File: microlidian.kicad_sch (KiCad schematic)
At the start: 31 parts, among them J1 Conn_02x05_Odd_Even, J11 Backboard Conn 1, J12 Frontboard Conn 1, J13 Backboard Conn 2, J14 Frontboard Conn 2, J2 ST7789 TFT socket, J3 Expansion header, J4 ADS1015 digital side, J5 ADS1015 analog side, J7 TRS MIDI Out, SW1 RotaryEncoder_Switch, SW2 Back button, U1 SeeeduinoXIAO, U2 L78L05_TO92

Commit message: some minor updates
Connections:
- net GND: no longer J5.5 (Pin_5)
- new net CV GND: J5.5 (Pin_5)
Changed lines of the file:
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@@
     )
   )
-  (global_label "CV GND" (shape input) (at 180.848 20.32 0) (fields_autoplaced)
+  (global_label "CV GND" (shape input) (at 200.406 20.32 0) (fields_autoplaced)
     (effects (font (size 1.27 1.27)) (justify left))
-    (property "Intersheetrefs" "${INTERSHEET_REFS}" (at 190.0907 20.32 0)
+    (property "Intersheetrefs" "${INTERSHEET_REFS}" (at 209.6487 20.32 0)
       (effects (font (size 1.27 1.27)) (justify left) hide)
     )

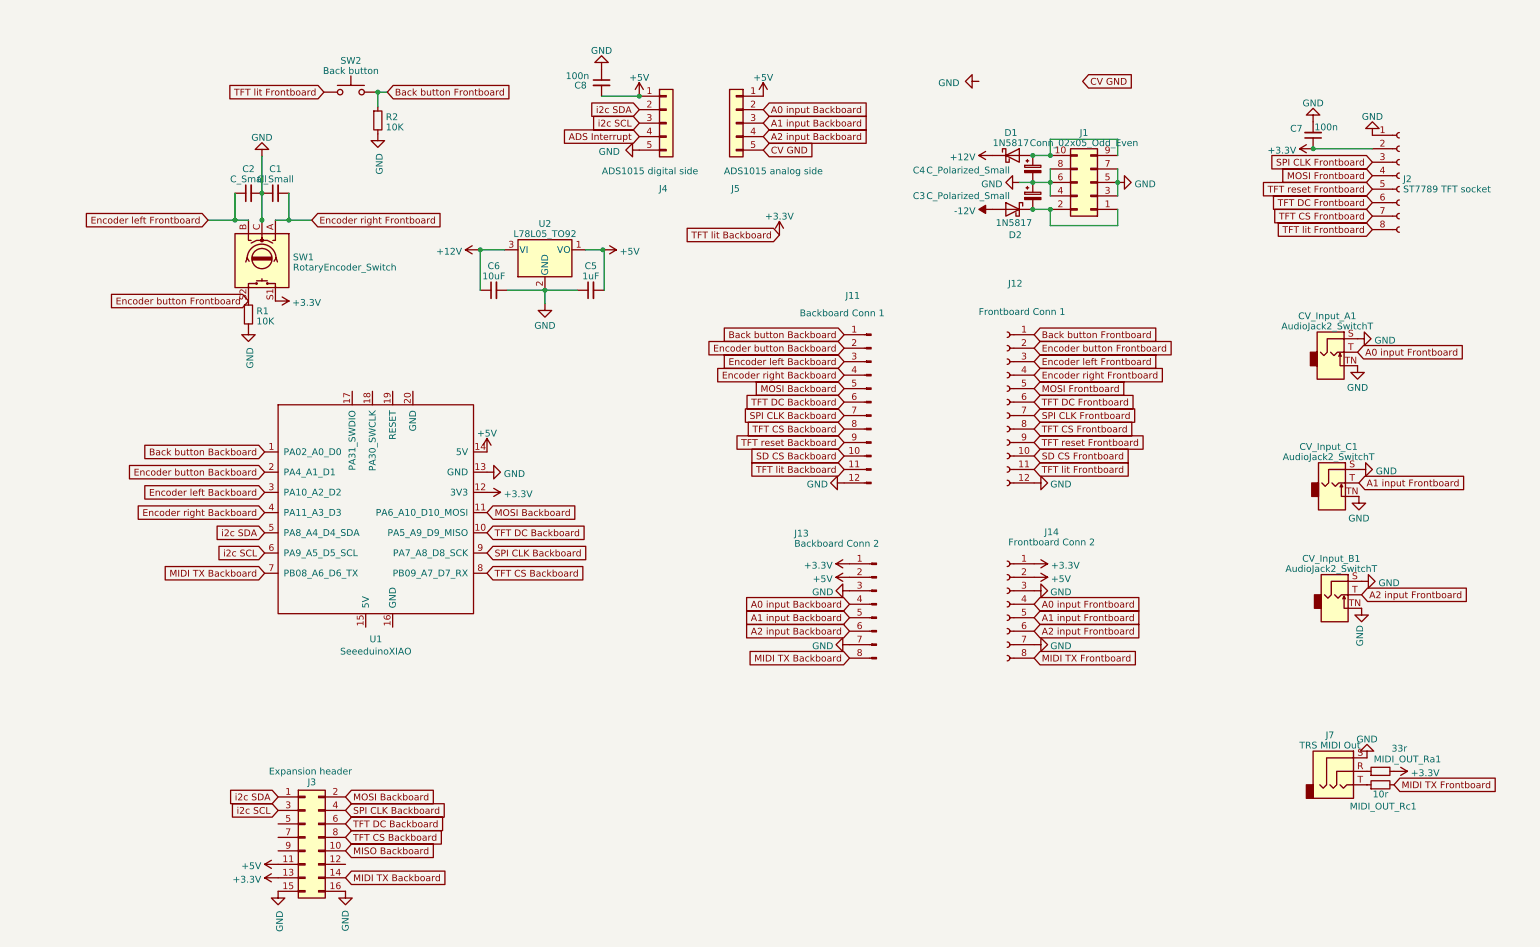
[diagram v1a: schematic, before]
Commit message: separated frontboard backboard gnds and +3.3v/+5v.  haven't updated pcb at all to match, yet
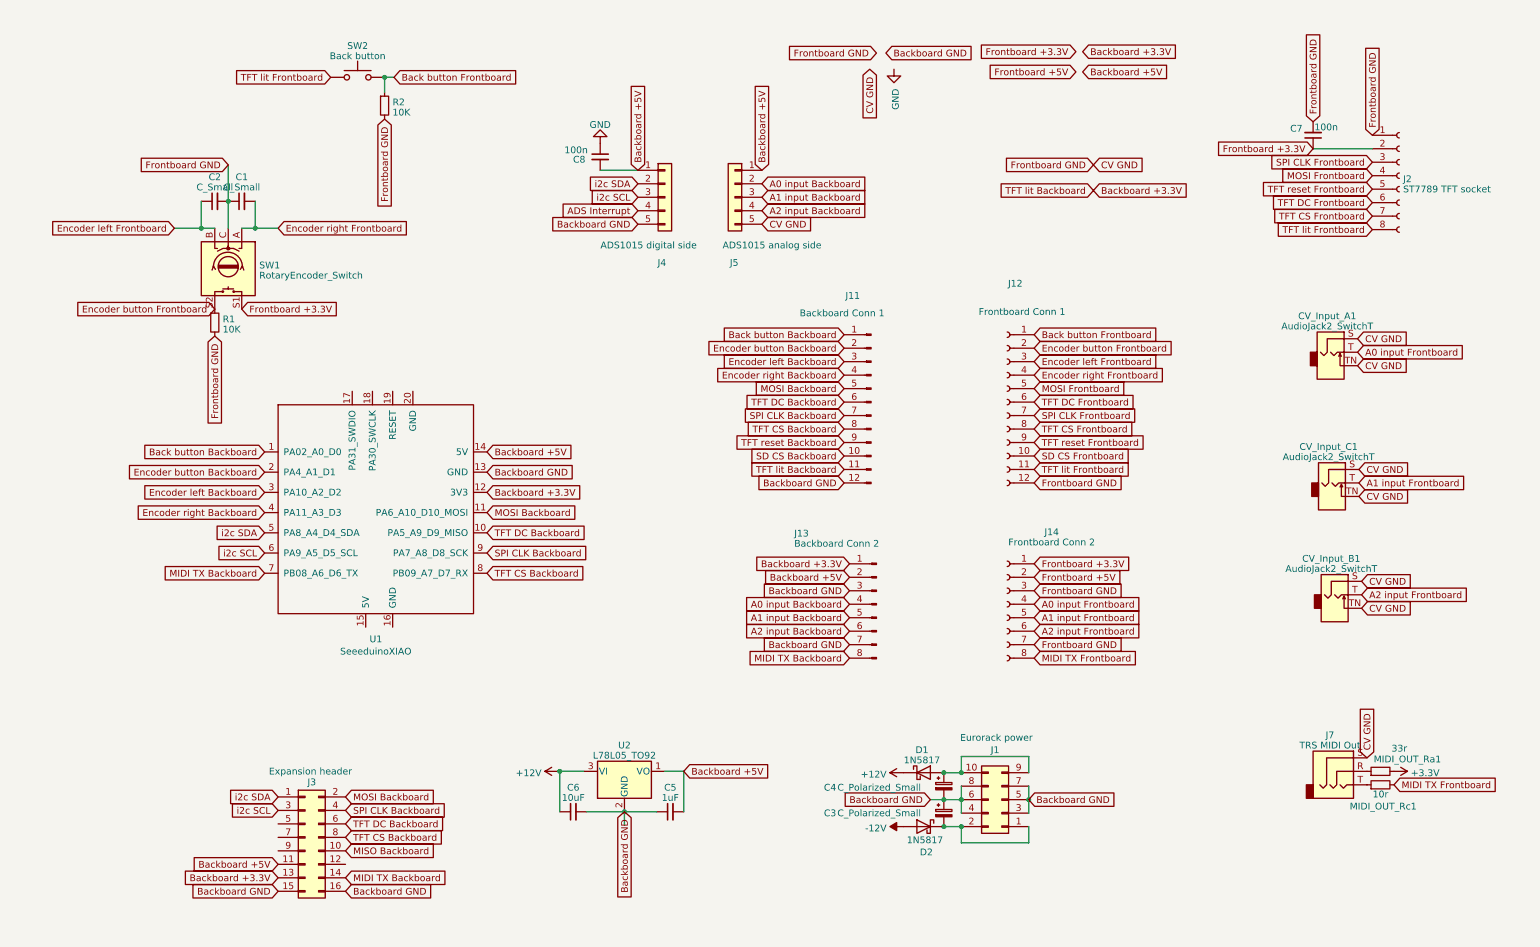
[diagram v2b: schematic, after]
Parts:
- J1: value Conn_02x05_Odd_Even -> Eurorack power
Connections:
- net +3.3V: no longer C7.1, J11.11 (Pin_11), J13.1 (Pin_1), J14.1 (Pin_1), J2.2 (Pin_2), J3.13 (Pin_13), SW1.S1, U1.12 (3V3)
- net CV GND: now also C1.1, C2.2, C7.2, CV_Input_A1.S, CV_Input_A1.TN, CV_Input_B1.S, CV_Input_B1.TN, CV_Input_C1.S, CV_Input_C1.TN, J12.12 (Pin_12), J14.3 (Pin_3), J14.7 (Pin_7), J2.1 (Pin_1), J7.S, R1.2, R2.2, SW1.C
- net GND: no longer C1.1, C2.2, C3.1, C4.2, C5.1, C6.2, C7.2, CV_Input_A1.S, CV_Input_A1.TN, CV_Input_B1.S, CV_Input_B1.TN, CV_Input_C1.S, CV_Input_C1.TN, J1.3 (Pin_3), J1.4 (Pin_4), J1.5 (Pin_5), J1.6 (Pin_6), J1.7 (Pin_7), J1.8 (Pin_8), J11.12 (Pin_12), J12.12 (Pin_12), J13.3 (Pin_3), J13.7 (Pin_7), J14.3 (Pin_3), J14.7 (Pin_7), J2.1 (Pin_1), J3.15 (Pin_15), J3.16 (Pin_16), J4.5 (Pin_5), J7.S, R1.2, R2.2, SW1.C, U1.13 (GND), U2.2 (GND)
- net +5V renamed Backboard +5V
- net Backboard +5V: no longer J14.2 (Pin_2)
- new net Backboard +3.3V: J11.11 (Pin_11), J13.1 (Pin_1), J3.13 (Pin_13), U1.12 (3V3)
- new net Backboard GND: C3.1, C4.2, C5.1, C6.2, J1.3 (Pin_3), J1.4 (Pin_4), J1.5 (Pin_5), J1.6 (Pin_6), J1.7 (Pin_7), J1.8 (Pin_8), J11.12 (Pin_12), J13.3 (Pin_3), J13.7 (Pin_7), J3.15 (Pin_15), J3.16 (Pin_16), J4.5 (Pin_5), U1.13 (GND), U2.2 (GND)
- new net Frontboard +3.3V: C7.1, J14.1 (Pin_1), J2.2 (Pin_2), SW1.S1
- new net Frontboard +5V: J14.2 (Pin_2)
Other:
- moved on the sheet: C1, C2, C3, C4, C5, C6, C8, D1, D2, J1, J4, J5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

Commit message: completely relaid out the pcb
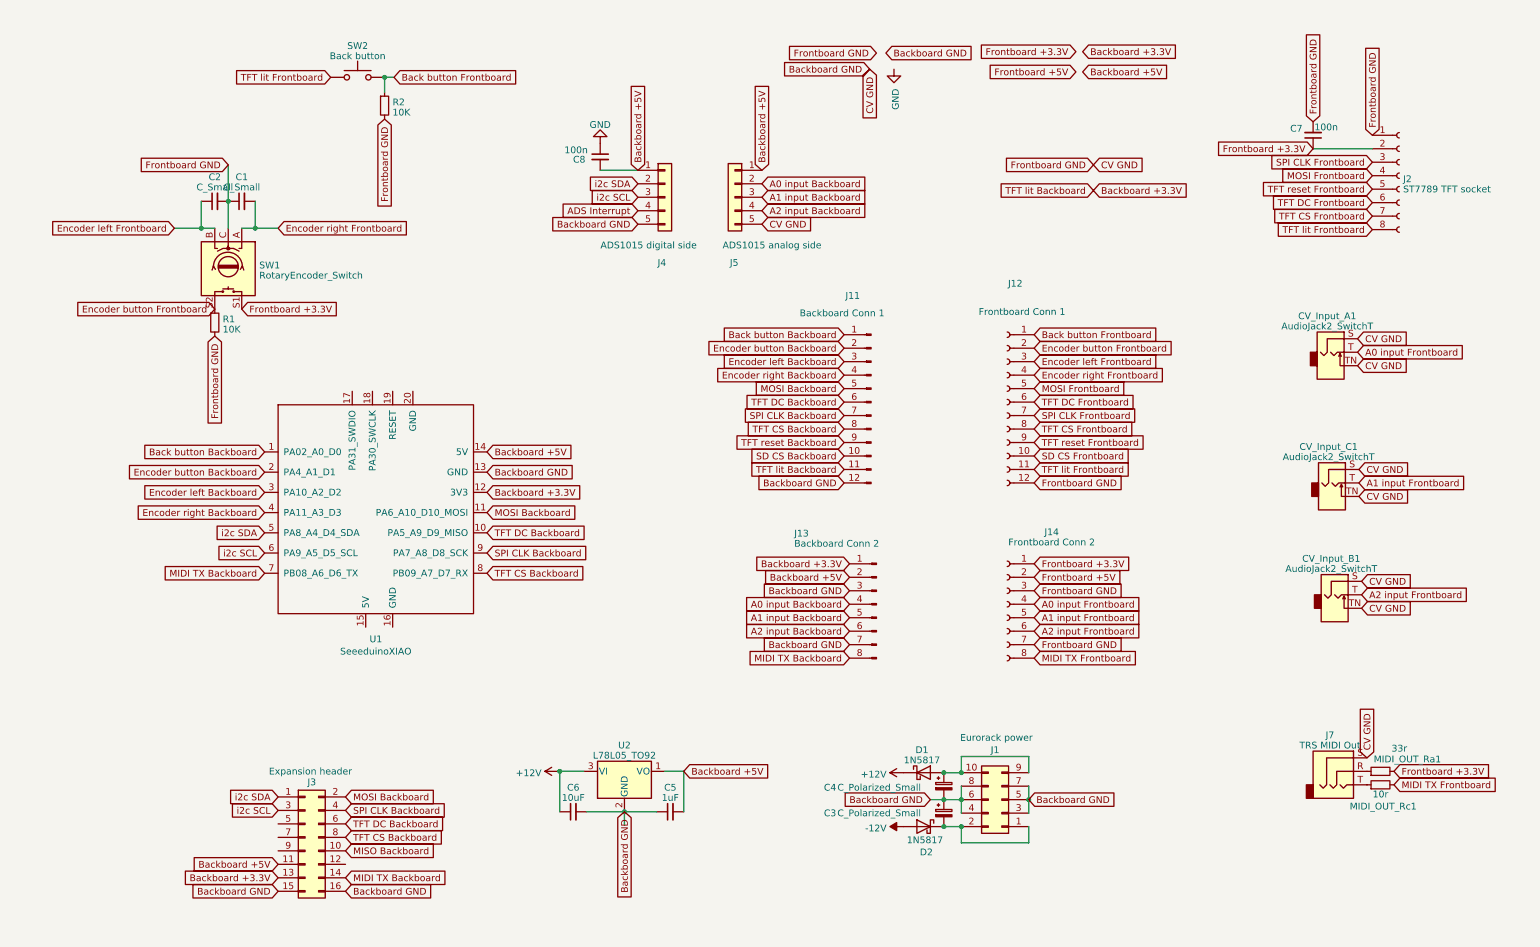
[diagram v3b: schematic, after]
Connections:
- net +3.3V is gone; now on net Frontboard +3.3V: MIDI_OUT_Ra1.2
- net CV GND is gone; now on net Backboard GND: C1.1, C2.2, C7.2, CV_Input_A1.S, CV_Input_A1.TN, CV_Input_B1.S, CV_Input_B1.TN, CV_Input_C1.S, CV_Input_C1.TN, J12.12 (Pin_12), J14.3 (Pin_3), J14.7 (Pin_7), J2.1 (Pin_1), J5.5 (Pin_5), J7.S, R1.2, R2.2, SW1.C
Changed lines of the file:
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@@
+    )
+  )
+  (global_label "Frontboard +3.3V" (shape input) (at 259.08 150.368 0) (fields_autoplaced)
+    (effects (font (size 1.27 1.27)) (justify left))
+    (property "Intersheetrefs" "${INTERSHEET_REFS}" (at 278.0591 150.368 0)
+      (effects (font (size 1.27 1.27)) (justify left) hide)
     )
   )
@@
     (effects (font (size 1.27 1.27)) (justify right))
     (property "Intersheetrefs" "${INTERSHEET_REFS}" (at 39.5982 19.558 0)
+      (effects (font (size 1.27 1.27)) (justify right) hide)
+    )
+  )
+  (global_label "Backboard GND" (shape input) (at 160.274 18.034 180) (fields_autoplaced)
+    (effects (font (size 1.27 1.27)) (justify right))
+    (property "Intersheetrefs" "${INTERSHEET_REFS}" (at 143.472 18.034 0)
       (effects (font (size 1.27 1.27)) (justify right) hide)
     )
@@
         )
       )
-    )
-  )
-  (symbol (lib_id "power:+3.3V") (at 259.08 150.368 270) (unit 1)
-    (in_bom yes) (on_board yes) (dnp no) (fields_autoplaced)
-    (property "Reference" "#PWR020" (at 255.27 150.368 0)
-      (effects (font (size 1.27 1.27)) hide)
-    )
-    (property "Value" "+3.3V" (at 262.255 150.6848 90)
-      (effects (font (size 1.27 1.27)) (justify left))
-    )
-    (property "Footprint" "" (at 259.08 150.368 0)
-      (effects (font (size 1.27 1.27)) hide)
-    )
-    (property "Datasheet" "" (at 259.08 150.368 0)
-      (effects (font (size 1.27 1.27)) hide)
-    )
-    (pin "1")
-    (instances
-      (project "microlidian"
-        (path "/f3b5c3e2-a769-4f71-bc6f-5b90415c45e5"
-          (reference "#PWR020") (unit 1)
-        )
-      )

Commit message: added pullup on RES, think this actually fixes power on screen problem!! :D
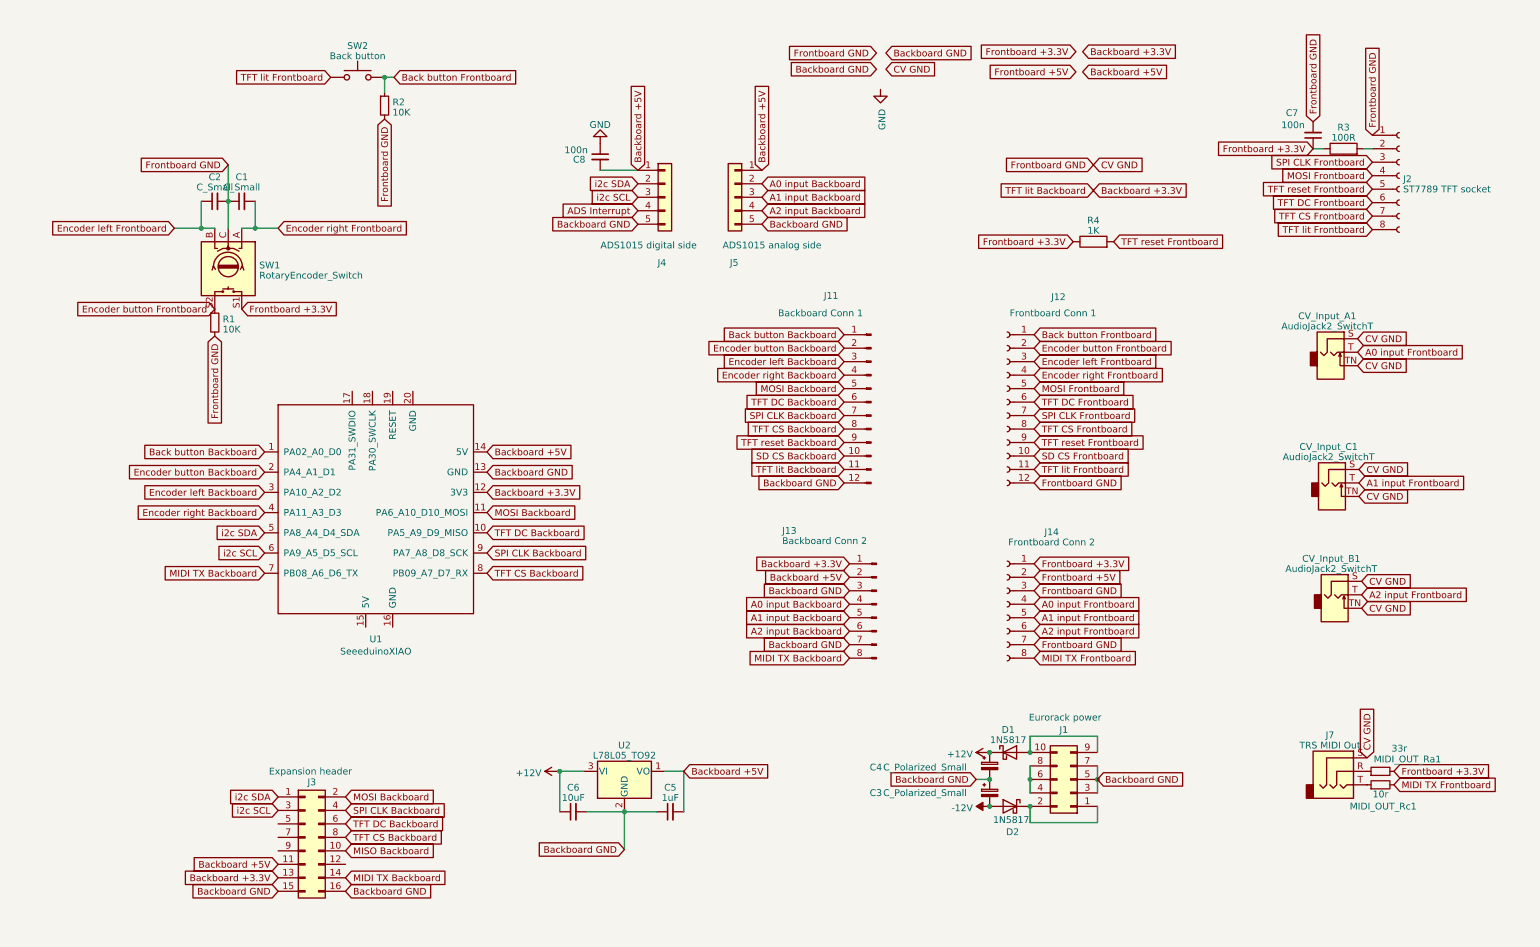
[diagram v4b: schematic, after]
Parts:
- added R3: 100R, Resistor_THT:R_Axial_DIN0207_L6.3mm_D2.5mm_P7.62mm_Horizontal, symbol Device:R
- added R4: 1K, Resistor_THT:R_Axial_DIN0207_L6.3mm_D2.5mm_P7.62mm_Horizontal, symbol Device:R
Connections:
- net +12V: now also C4.1
- net -12V: now also C3.2
- net Backboard GND: no longer C1.1, C2.2, C7.2, CV_Input_A1.S, CV_Input_A1.TN, CV_Input_B1.S, CV_Input_B1.TN, CV_Input_C1.S, CV_Input_C1.TN, J1.4 (Pin_4), J1.6 (Pin_6), J1.8 (Pin_8), J12.12 (Pin_12), J14.3 (Pin_3), J14.7 (Pin_7), J2.1 (Pin_1), J7.S, R1.2, R2.2, SW1.C
- net Frontboard +3.3V: now also R3.1, R4.1; no longer J2.2 (Pin_2)
- net TFT reset Frontboard: now also R4.2
- net at D1.2 (A), J1.10 (Pin_10), J1.9 (Pin_9): no longer C4.1
- net at D2.1 (K), J1.1 (Pin_1), J1.2 (Pin_2): no longer C3.2
- new net: J2.2 (Pin_2), R3.2
- new net: J1.4 (Pin_4), J1.6 (Pin_6), J1.8 (Pin_8)
- new net CV GND: C1.1, C2.2, C7.2, CV_Input_A1.S, CV_Input_A1.TN, CV_Input_B1.S, CV_Input_B1.TN, CV_Input_C1.S, CV_Input_C1.TN, J12.12 (Pin_12), J14.3 (Pin_3), J14.7 (Pin_7), J2.1 (Pin_1), J7.S, R1.2, R2.2, SW1.C
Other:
- moved on the sheet: C3, C4, D1, D2, J1

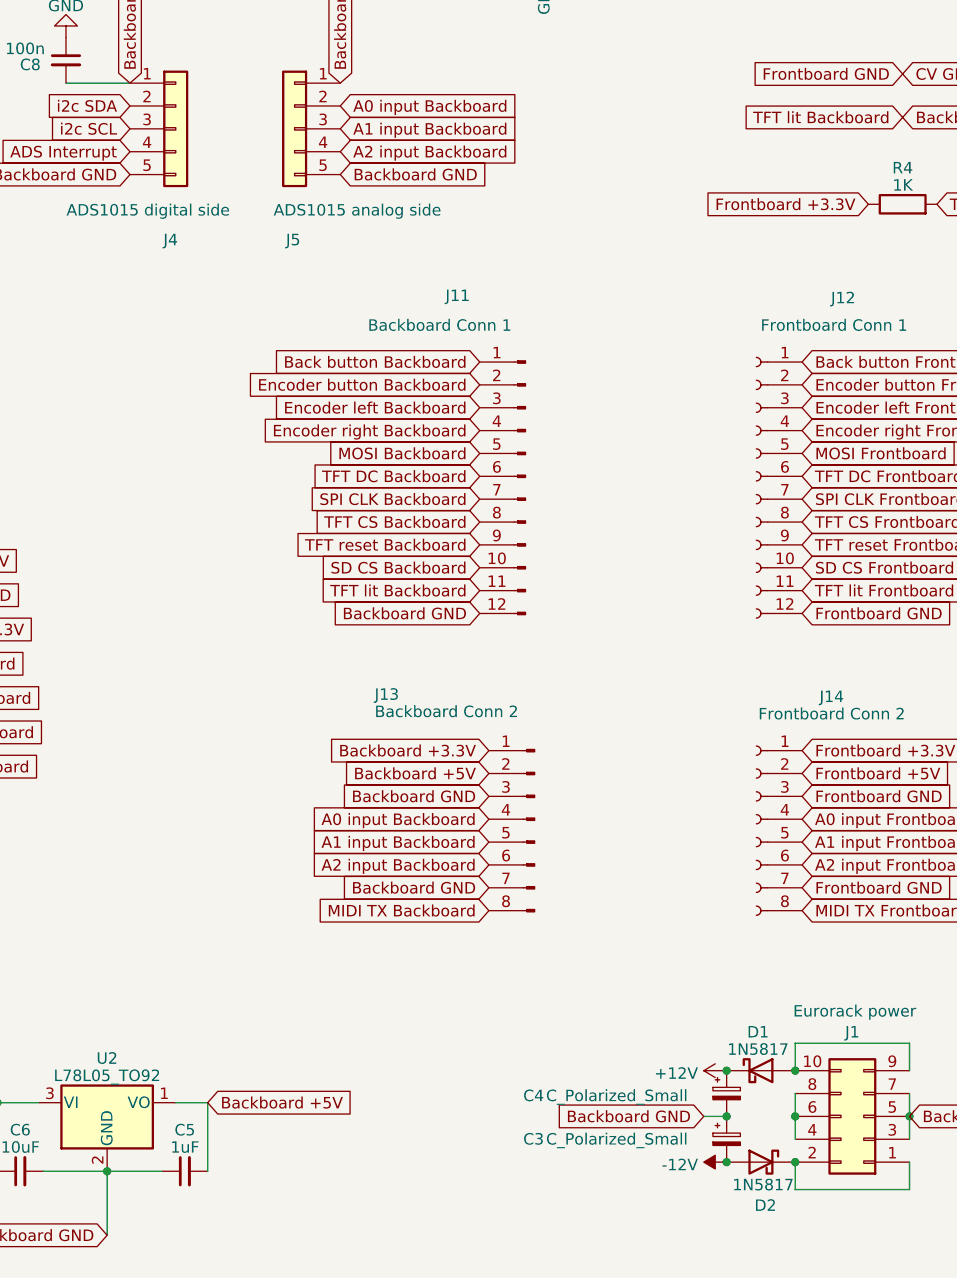
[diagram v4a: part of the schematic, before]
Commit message: fixed connection to ground
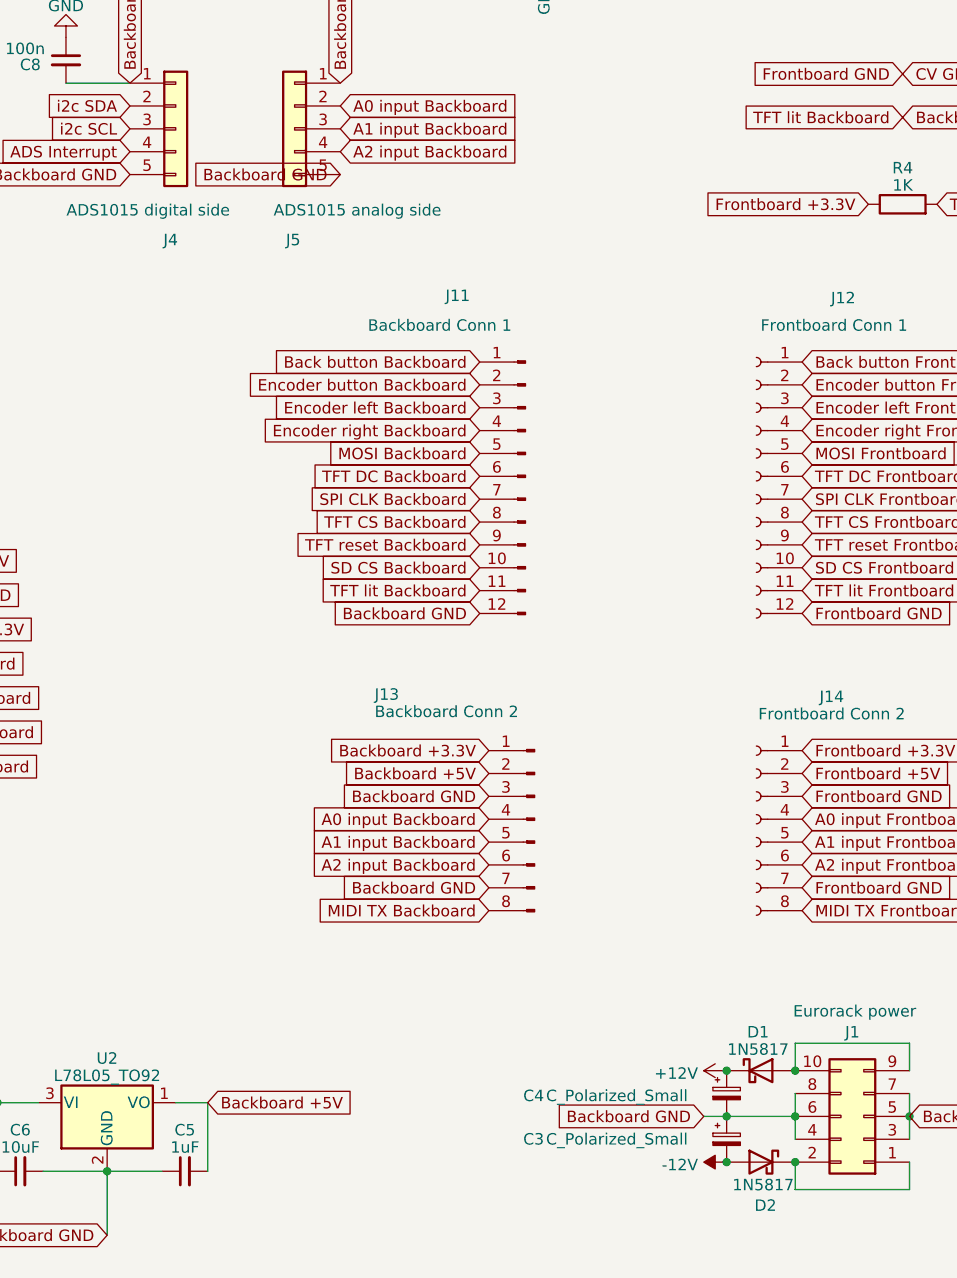
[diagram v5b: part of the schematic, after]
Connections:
- net Backboard GND: now also J1.4 (Pin_4), J1.6 (Pin_6), J1.8 (Pin_8)
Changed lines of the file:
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@@
+    (stroke (width 0) (type default))
+  )
+  (wire (pts (xy 182.88 151.892) (xy 190.5 151.892))
     (stroke (width 0) (type default))
   )
@@
     )
   )
-  (global_label "Backboard GND" (shape input) (at 139.954 47.244 0) (fields_autoplaced)
-    (effects (font (size 1.27 1.27)) (justify left))
-    (property "Intersheetrefs" "${INTERSHEET_REFS}" (at 156.9616 47.244 0)
-      (effects (font (size 1.27 1.27)) (justify left) hide)
-    )
-  )
+  (global_label "Backboard GND" (shape input) (at 139.954 47.244 180) (fields_autoplaced)
+    (effects (font (size 1.27 1.27)) (justify right))
+    (property "Intersheetrefs" "${INTERSHEET_REFS}" (at 122.9464 47.244 0)
+      (effects (font (size 1.27 1.27)) (justify right) hide)
+    )
+  )
